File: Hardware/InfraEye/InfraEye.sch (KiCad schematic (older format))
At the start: 3 parts

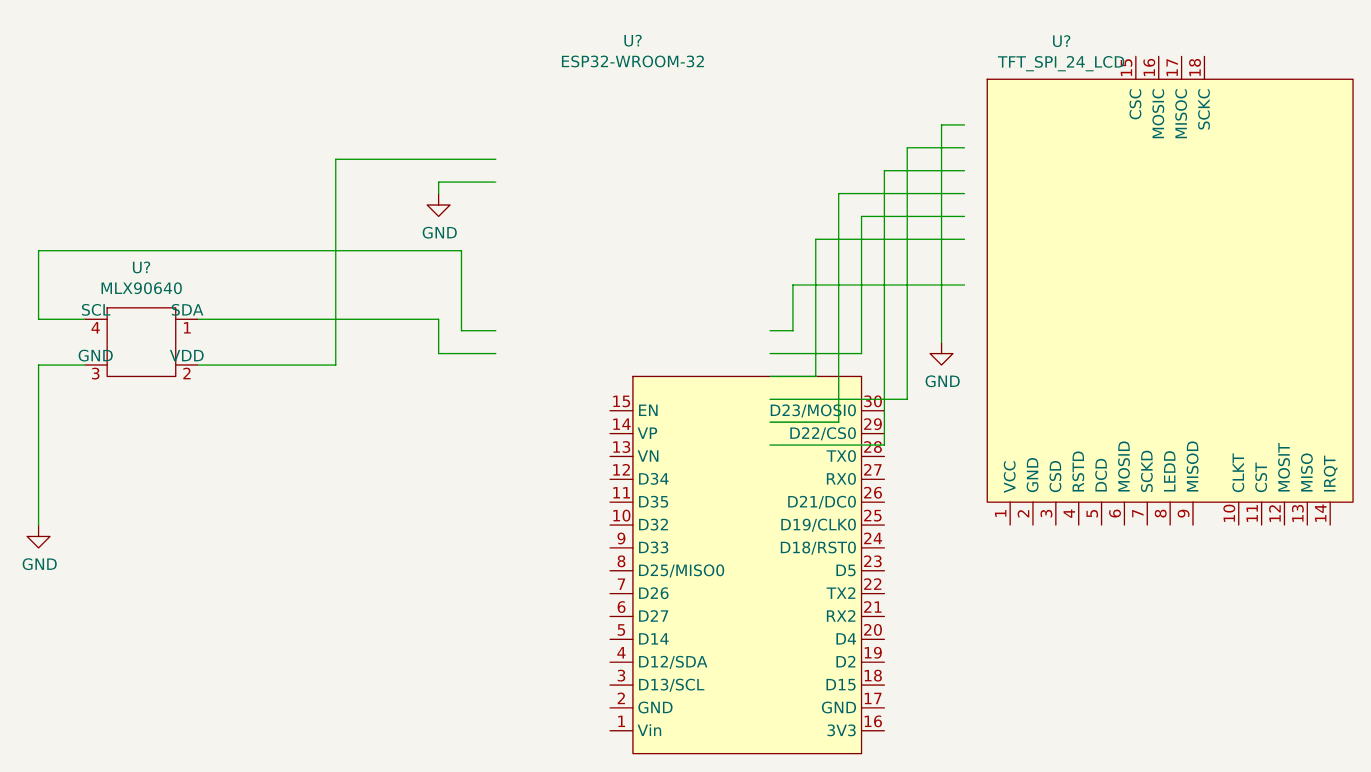
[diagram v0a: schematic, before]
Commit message: Added footprints for LCD, ESP32 board and IR sensor
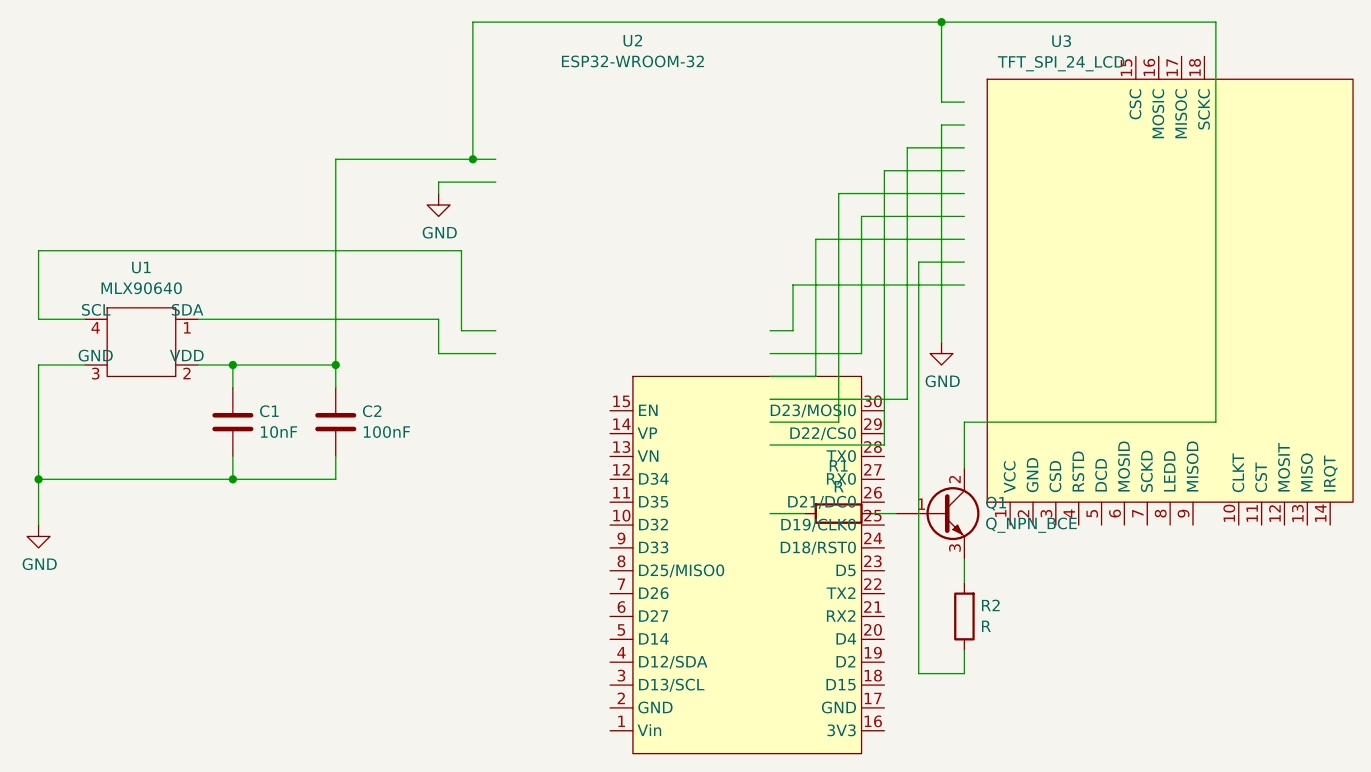
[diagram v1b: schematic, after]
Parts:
- added C1: 10nF, OLIMEX_RLC-FP:C_1206_5MIL_DWS_ISO, symbol Device:C
- added C2: 100nF, OLIMEX_RLC-FP:C_1206_5MIL_DWS_ISO, symbol Device:C
- added Q1: Q_NPN_BCE, OLIMEX_Diodes-FP:SOT23-3, symbol Device:Q_NPN_BCE
- added R1, R2: R, OLIMEX_RLC-FP:R_1206_5MIL_DWS_ISO, symbol Device:R
- U1: renamed from U?; footprint (none) -> InfraEye:MLX90614
- U2: renamed from U?; footprint RF_Module:ESP32-WROOM-32 -> InfraEye:ESP32-WROOM-32-30pin
- U3: renamed from U?; footprint (none) -> InfraEye:TFT_LCD_24
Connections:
- wire segments 35 -> 59
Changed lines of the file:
@@
 $EndDescr
 $Comp
-L InfraEye:MLX90640 U?
+L InfraEye:MLX90640 U1
 U 1 1 5E2A1863
 P 2800 3150
-F 0 "U?" H 2950 3325 50  0000 C CNN
+F 0 "U1" H 2950 3325 50  0000 C CNN
 F 1 "MLX90640" H 2950 3234 50  0000 C CNN
-F 2 "" H 2850 3300 50  0001 C CNN
+F 2 "InfraEye:MLX90614" H 2850 3300 50  0001 C CNN
 F 3 "" H 2850 3300 50  0001 C CNN
 	1    2800 3150
@@
 $EndComp
 $Comp
-L InfraEye:ESP32-WROOM-32 U?
+L InfraEye:ESP32-WROOM-32 U2
 U 1 1 5E2A6228
 P 5100 3450
-F 0 "U?" H 5100 4917 50  0000 C CNN
+F 0 "U2" H 5100 4917 50  0000 C CNN
 F 1 "ESP32-WROOM-32" H 5100 4826 50  0000 C CNN
-F 2 "RF_Module:ESP32-WROOM-32" H 5100 1950 50  0001 C CNN
+F 2 "InfraEye:ESP32-WROOM-32-30pin" H 5100 1950 50  0001 C CNN
 F 3 "" H 4800 3500 50  0001 C CNN
 	1    5100 3450
@@
 $EndComp
 $Comp
-L InfraEye:TFT_SPI_24_LCD U?
+L InfraEye:TFT_SPI_24_LCD U3
 U 1 1 5E2A99BF
 P 6650 2150
-F 0 "U?" H 6975 2315 50  0000 C CNN
+F 0 "U3" H 6975 2315 50  0000 C CNN
 F 1 "TFT_SPI_24_LCD" H 6975 2224 50  0000 C CNN
-F 2 "" H 8900 2100 50  0001 C CNN
+F 2 "InfraEye:TFT_LCD_24" H 8900 2100 50  0001 C CNN
 F 3 "" H 8900 2100 50  0001 C CNN
 	1    6650 2150
@@
 $EndComp
 $Comp
-L power:GND #PWR?
+L power:GND #PWR01
 U 1 1 5E2ACB51
 P 2500 4100
-F 0 "#PWR?" H 2500 3850 50  0001 C CNN
+F 0 "#PWR01" H 2500 3850 50  0001 C CNN
 F 1 "GND" H 2505 3927 50  0000 C CNN
 F 2 "" H 2500 4100 50  0001 C CNN
@@
 $EndComp
 Wire Wire Line
-	3200 3400 3800 3400
+	3200 3400 3350 3400
 Wire Wire Line
 	3800 3400 3800 2500
 Wire Wire Line
-	3800 2500 4500 2500
-Wire Wire Line
-	2500 4100 2500 3400
+	3800 2500 4400 2500
+Wire Wire Line
+	2500 4100 2500 3900
 Wire Wire Line
 	2500 3400 2700 3400
@@
 	4350 3250 4500 3250
 $Comp
-L power:GND #PWR?
+L power:GND #PWR02
 U 1 1 5E2AF47D
 P 4250 2650
-F 0 "#PWR?" H 4250 2400 50  0001 C CNN
+F 0 "#PWR02" H 4250 2400 50  0001 C CNN
 F 1 "GND" H 4255 2477 50  0000 C CNN
 F 2 "" H 4250 2650 50  0001 C CNN
@@
 $EndComp
 $Comp
-L power:GND #PWR?
+L power:GND #PWR03
 U 1 1 5E2AFA8C
 P 6450 3300
-F 0 "#PWR?" H 6450 3050 50  0001 C CNN
+F 0 "#PWR03" H 6450 3050 50  0001 C CNN
 F 1 "GND" H 6455 3127 50  0000 C CNN
 F 2 "" H 6450 3300 50  0001 C CNN
@@
 Wire Wire Line
 	6300 3550 5700 3550
+$Comp
+L Device:C C1
+U 1 1 5E2B3FCF
+P 3350 3650
+F 0 "C1" H 3465 3696 50  0000 L CNN
+F 1 "10nF" H 3465 3605 50  0000 L CNN
+F 2 "OLIMEX_RLC-FP:C_1206_5MIL_DWS_ISO" H 3388 3500 50  0001 C CNN
+F 3 "~" H 3350 3650 50  0001 C CNN
+	1    3350 3650
+	1    0    0    -1
+$EndComp
+$Comp
+L Device:C C2
+U 1 1 5E2B489C
+P 3800 3650
+F 0 "C2" H 3915 3696 50  0000 L CNN
+F 1 "100nF" H 3915 3605 50  0000 L CNN
+F 2 "OLIMEX_RLC-FP:C_1206_5MIL_DWS_ISO" H 3838 3500 50  0001 C CNN
+F 3 "~" H 3800 3650 50  0001 C CNN
+	1    3800 3650
+	1    0    0    -1
+$EndComp
+Wire Wire Line
+	3800 3500 3800 3400
+Connection ~ 3800 3400
+Wire Wire Line
+	3350 3500 3350 3400
+Connection ~ 3350 3400
+Wire Wire Line
+	3350 3400 3800 3400
+Wire Wire Line
+	3350 3800 3350 3900
+Wire Wire Line
+	3350 3900 2500 3900
+Connection ~ 2500 3900
+Wire Wire Line
+	2500 3900 2500 3400
+Wire Wire Line
+	3800 3800 3800 3900
+Wire Wire Line
+	3800 3900 3350 3900
+Connection ~ 3350 3900
+$Comp
+L Device:R R1
+U 1 1 5E2B9457
+P 6000 4050
+F 0 "R1" V 5793 4050 50  0000 C CNN
+F 1 "R" V 5884 4050 50  0000 C CNN
+F 2 "OLIMEX_RLC-FP:R_1206_5MIL_DWS_ISO" V 5930 4050 50  0001 C CNN
+F 3 "~" H 6000 4050 50  0001 C CNN
+	1    6000 4050
+	0    1    1    0
+$EndComp
+$Comp
+L Device:Q_NPN_BCE Q1
+U 1 1 5E2BA2F2
+P 6450 4050
+F 0 "Q1" H 6641 4096 50  0000 L CNN
+F 1 "Q_NPN_BCE" H 6641 4005 50  0000 L CNN
+F 2 "OLIMEX_Diodes-FP:SOT23-3" H 6650 4150 50  0001 C CNN
+F 3 "~" H 6450 4050 50  0001 C CNN
+	1    6450 4050
+	1    0    0    -1
+$EndComp
+$Comp
+L Device:R R2
+U 1 1 5E2BB6A2
+P 6550 4500
+F 0 "R2" H 6480 4454 50  0000 R CNN
+F 1 "R" H 6480 4545 50  0000 R CNN
+F 2 "OLIMEX_RLC-FP:R_1206_5MIL_DWS_ISO" V 6480 4500 50  0001 C CNN
+F 3 "~" H 6550 4500 50  0001 C CNN
+	1    6550 4500
+	-1   0    0    1
+$EndComp
+Wire Wire Line
+	6550 2250 6450 2250
+Wire Wire Line
+	6450 2250 6450 1900
+Wire Wire Line
+	6450 1900 4400 1900
+Wire Wire Line
+	4400 1900 4400 2500
+Connection ~ 4400 2500
+Wire Wire Line
+	4400 2500 4500 2500
+Wire Wire Line
+	6550 2950 6350 2950
+Wire Wire Line
+	6350 2950 6350 4750
+Wire Wire Line
+	6350 4750 6550 4750
+Wire Wire Line
+	6550 4750 6550 4650
+Wire Wire Line
+	6550 4350 6550 4250
+Wire Wire Line
+	6250 4050 6150 4050
+Wire Wire Line
+	5850 4050 5700 4050
+Wire Wire Line
+	6450 1900 7650 1900
+Wire Wire Line
+	7650 1900 7650 3650
+Wire Wire Line
+	7650 3650 6550 3650
+Wire Wire Line
+	6550 3650 6550 3850
+Connection ~ 6450 1900
 $EndSCHEMATC

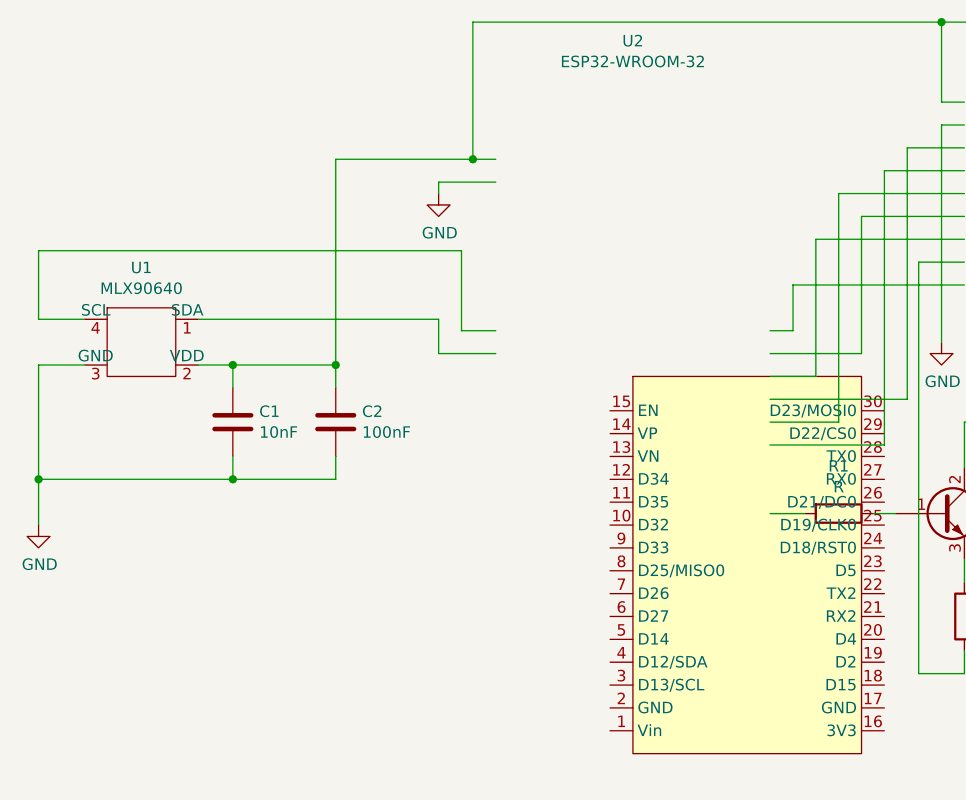
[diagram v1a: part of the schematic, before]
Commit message: PCB: Added second IR sensor - LCD/WIFI version will have IR sensor placed on different places of PCB. SW: Changed pins of SPI buses, LCD moved to VSPI bus and speed increased to 60MHz, touch sensor moved to HSPI bus and speed decreased to 125kHz. Some changes done to reading from touch sensor, some data that correspond to screen touching are present on bus, but data still doesn't give coordinates.
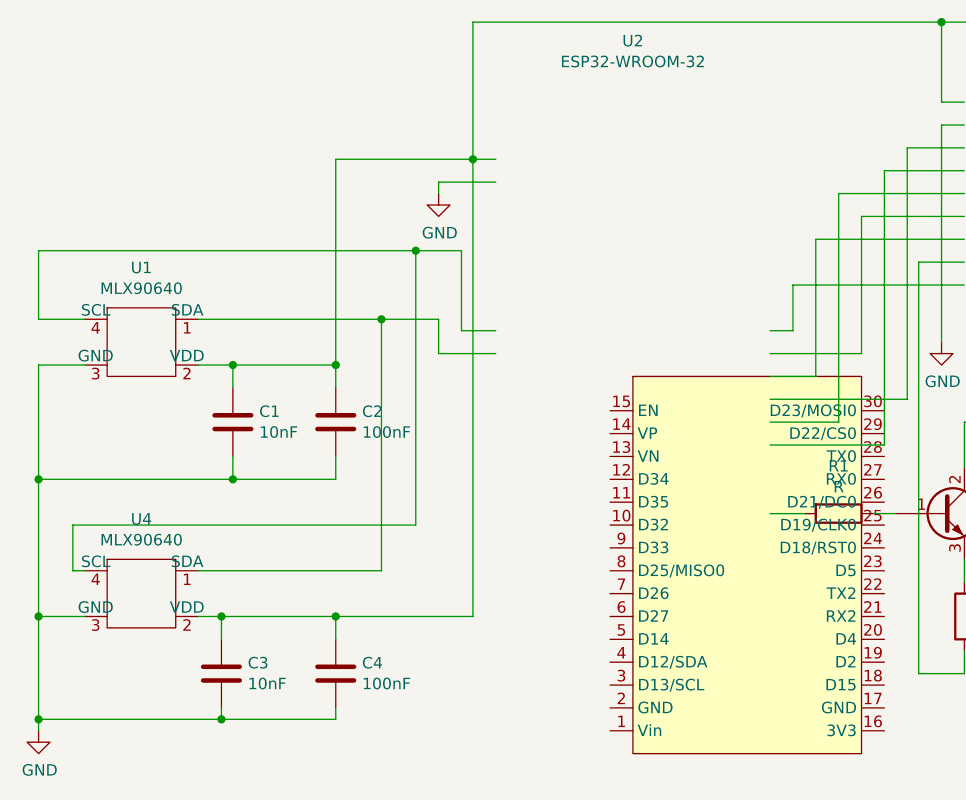
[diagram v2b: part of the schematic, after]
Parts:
- added C3: 10nF, OLIMEX_RLC-FP:C_1206_5MIL_DWS_ISO, symbol Device:C
- added C4: 100nF, OLIMEX_RLC-FP:C_1206_5MIL_DWS_ISO, symbol Device:C
- added U4: MLX90640, InfraEye:MLX90614, symbol InfraEye:MLX90640
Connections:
- wire segments 59 -> 80
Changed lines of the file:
@@
 L power:GND #PWR01
 U 1 1 5E2ACB51
-P 2500 4100
-F 0 "#PWR01" H 2500 3850 50  0001 C CNN
-F 1 "GND" H 2505 3927 50  0000 C CNN
-F 2 "" H 2500 4100 50  0001 C CNN
-F 3 "" H 2500 4100 50  0001 C CNN
-	1    2500 4100
+P 2500 5000
+F 0 "#PWR01" H 2500 4750 50  0001 C CNN
+F 1 "GND" H 2505 4827 50  0000 C CNN
+F 2 "" H 2500 5000 50  0001 C CNN
+F 3 "" H 2500 5000 50  0001 C CNN
+	1    2500 5000
 	1    0    0    -1
 $EndComp
@@
 	3800 2500 4400 2500
 Wire Wire Line
-	2500 4100 2500 3900
-Wire Wire Line
 	2500 3400 2700 3400
 Wire Wire Line
-	3200 3200 4250 3200
+	3200 3200 4000 3200
 Wire Wire Line
 	4250 3200 4250 3350
@@
 	2500 3200 2500 2900
 Wire Wire Line
-	2500 2900 4350 2900
+	2500 2900 4150 2900
 Wire Wire Line
 	4350 2900 4350 3250
@@
 	6250 4050 6150 4050
 Wire Wire Line
-	5850 4050 5700 4050
-Wire Wire Line
 	6450 1900 7650 1900
 Wire Wire Line
@@
 	6550 3650 6550 3850
 Connection ~ 6450 1900
+Wire Wire Line
+	5700 4050 5850 4050
+$Comp
+L InfraEye:MLX90640 U4
+U 1 1 5E336D8C
+P 2800 4250
+F 0 "U4" H 2950 4425 50  0000 C CNN
+F 1 "MLX90640" H 2950 4334 50  0000 C CNN
+F 2 "InfraEye:MLX90614" H 2850 4400 50  0001 C CNN
+F 3 "" H 2850 4400 50  0001 C CNN
+	1    2800 4250
+	1    0    0    -1
+$EndComp
+$Comp
+L Device:C C3
+U 1 1 5E337496
+P 3300 4750
+F 0 "C3" H 3415 4796 50  0000 L CNN
+F 1 "10nF" H 3415 4705 50  0000 L CNN
+F 2 "OLIMEX_RLC-FP:C_1206_5MIL_DWS_ISO" H 3338 4600 50  0001 C CNN
+F 3 "~" H 3300 4750 50  0001 C CNN
+	1    3300 4750
+	1    0    0    -1
+$EndComp
+$Comp
+L Device:C C4
+U 1 1 5E337BD5
+P 3800 4750
+F 0 "C4" H 3915 4796 50  0000 L CNN
+F 1 "100nF" H 3915 4705 50  0000 L CNN
+F 2 "OLIMEX_RLC-FP:C_1206_5MIL_DWS_ISO" H 3838 4600 50  0001 C CNN
+F 3 "~" H 3800 4750 50  0001 C CNN
+	1    3800 4750
+	1    0    0    -1
+$EndComp
+Wire Wire Line
+	3200 4300 4000 4300
+Wire Wire Line
+	4000 4300 4000 3200
+Connection ~ 4000 3200
+Wire Wire Line
+	4000 3200 4250 3200
+Wire Wire Line
+	2700 4300 2650 4300
+Wire Wire Line
+	2650 4300 2650 4100
+Wire Wire Line
+	2650 4100 4150 4100
+Wire Wire Line
+	4150 4100 4150 2900
+Connection ~ 4150 2900
+Wire Wire Line
+	4150 2900 4350 2900
+Wire Wire Line
+	2500 3900 2500 4500
+Wire Wire Line
+	2700 4500 2500 4500
+Connection ~ 2500 4500
+Wire Wire Line
+	2500 4500 2500 4950
+Wire Wire Line
+	3800 4900 3800 4950
+Wire Wire Line
+	3800 4950 3300 4950
+Connection ~ 2500 4950
+Wire Wire Line
+	2500 4950 2500 5000
+Wire Wire Line
+	3300 4900 3300 4950
+Connection ~ 3300 4950
+Wire Wire Line
+	3300 4950 2500 4950
+Wire Wire Line
+	3200 4500 3300 4500
+Wire Wire Line
+	3300 4500 3300 4600
+Wire Wire Line
+	3300 4500 3800 4500
+Wire Wire Line
+	3800 4500 3800 4600
+Connection ~ 3300 4500
+Wire Wire Line
+	3800 4500 4400 4500
+Wire Wire Line
+	4400 4500 4400 2500
+Connection ~ 3800 4500
 $EndSCHEMATC

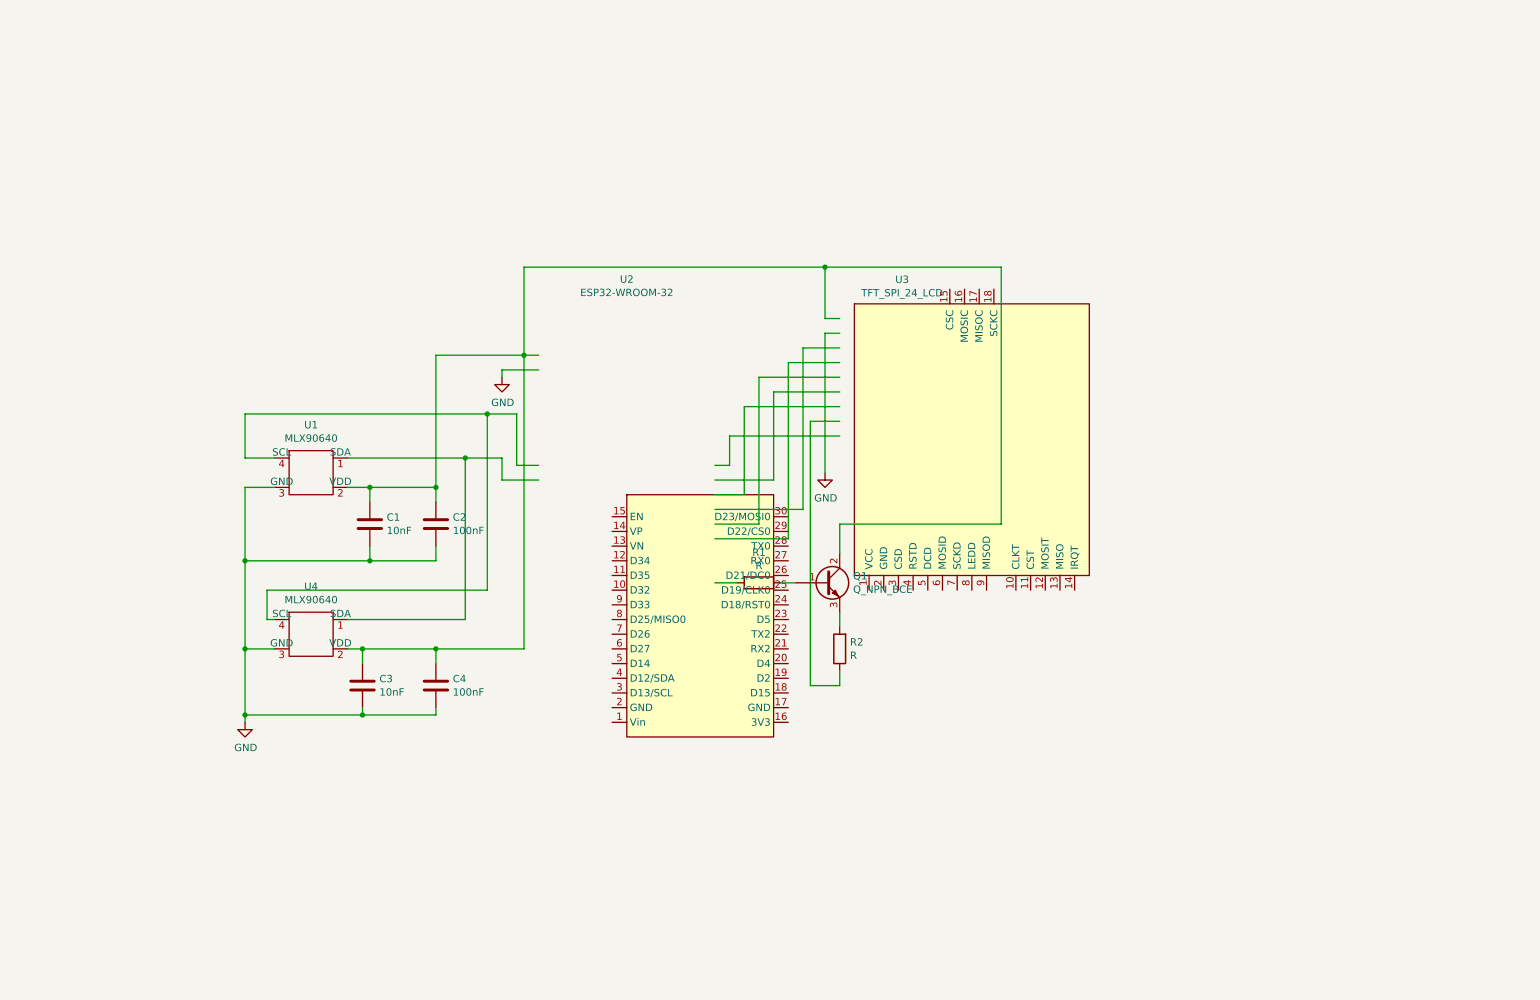
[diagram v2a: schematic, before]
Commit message: Reworked schematics and PCB - signals moved around to minimize signal crossings - not verified on HW if it works with remapped signals as on schematics.
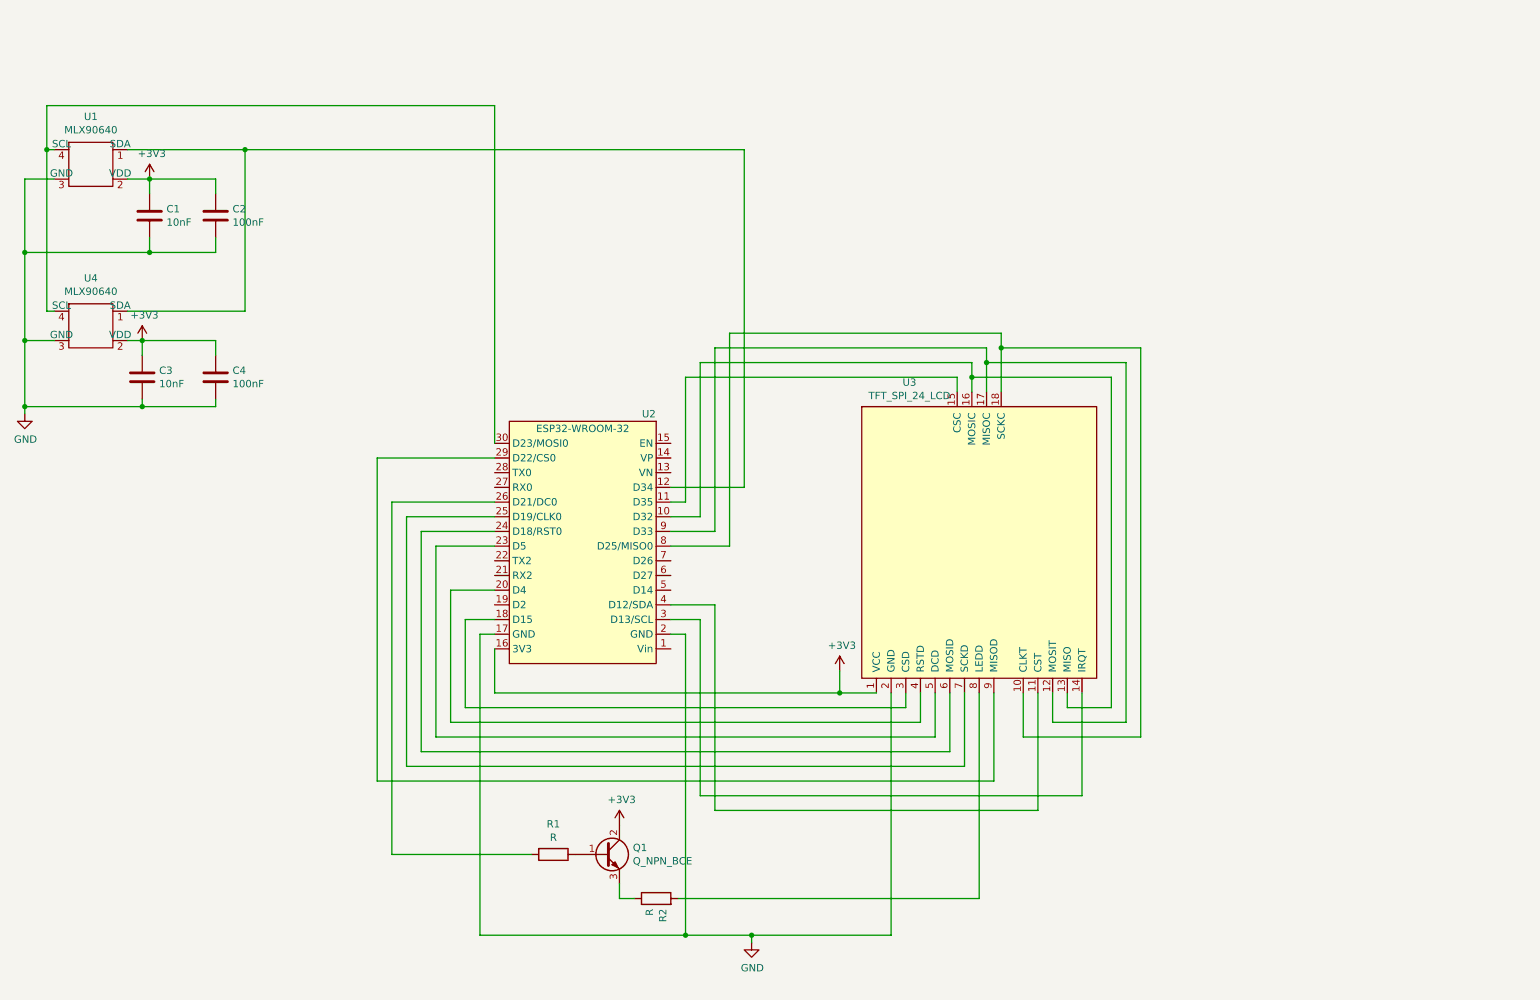
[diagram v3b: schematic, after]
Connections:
- net labels added: +3V3
- wire segments 80 -> 117
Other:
- moved on the sheet: C1, C2, C3, C4, Q1, R1, R2, U1, U2, U3, U4
